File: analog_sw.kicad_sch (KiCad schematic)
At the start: 22 parts, among them J5 Conn_02x05_Top_Bottom, Q3 BC817-25LT1G, Q4 BC817-25LT1G, Q5 BC817-25LT1G, Q6 BC817-25LT1G, U7 LTV-247

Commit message: Fix LED driver bias, add ST pull-ups, name TPS7B91 NC pins
- Swap LED driver base resistors: 2.2k series (R18/R20/R23/R26) and
  10k pull-down (R17/R21/R24/R27). The old 10k/2.2k divider only gave
  ~0.6 V at the base, so the NPNs never turned on.
- Add 10k pull-ups R29-R32 from IO2-IO5 to +3V3 for the open-drain ST
  outputs of the TPS1H100-Q1 switches on the output module.
- Name TPS7B91 pins 3 and 4 "NC" (datasheet: not internally connected).

ERC violation count unchanged (45, all pre-existing).

Co-Authored-By: Claude Opus 5.5 <noreply@anthropic.com>
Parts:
- R17, R21, R24, R27: value 2.2k -> 10k
- R18, R20, R23, R26: value 10k -> 2.2k
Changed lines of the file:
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@@
 			)
 		)
-		(property "Value" "2.2k"
+		(property "Value" "10k"
 			(at 135.128 72.898 0)
 			(effects
@@
 			)
 		)
-		(property "Value" "10k"
+		(property "Value" "2.2k"
 			(at 134.62 127 90)
 			(effects
@@
 			)
 		)
-		(property "Value" "2.2k"
+		(property "Value" "10k"
 			(at 135.128 137.668 0)
 			(effects
@@
 			)
 		)
-		(property "Value" "10k"
+		(property "Value" "2.2k"
 			(at 134.62 62.23 90)
 			(effects
@@
 			)
 		)
-		(property "Value" "2.2k"
+		(property "Value" "10k"
 			(at 135.128 41.148 0)
 			(effects
@@
 			)
 		)
-		(property "Value" "10k"
+		(property "Value" "2.2k"
 			(at 134.62 93.98 90)
 			(effects
@@
 			)
 		)
-		(property "Value" "10k"
+		(property "Value" "2.2k"
 			(at 134.62 30.48 90)
 			(effects
@@
 			)
 		)
-		(property "Value" "2.2k"
+		(property "Value" "10k"
 			(at 135.128 104.648 0)
 			(effects

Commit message: Apply JLCPCB BOM audit fixes and add module ID / switch sense
- Remove CH340C and auto-reset circuit; USB-C goes to native USB
  (IO19 = D-, IO20 = D+). UART0 left unconnected.
- USB-C: HRO TYPE-C-31-M-12 (shell pins renumbered SH to match footprint).
- F1/F3: 1812L050/60GR (60 V, 500 mA hold); old part was rated 30 V max.
- D2/D3/D11: DSK16 (60 V) replacing out-of-stock DSS14U.
- D9: PESD2CAN replacing unavailable ESDCAN01-2BWY (SOT-23).
- L1: SWPA6045S8R2MT (Isat 3.9 A > LMR51610 peak limit 1.95 A).
- Feedback divider 68k/22k (basic parts): Vout 3.27 V with Vref 0.8 V.
- Basic-library swaps: TS-1187A buttons, 0805 2.2uF/50V, 49.9 R,
  BC817-40.
- Move the ST pull-ups to the output module.
- Header pin 12 becomes MOD_ID (IO1, 10k pull-up).
- SW1-SW4 to IO14/IO15/IO16/IO21 with 10k pull-downs, so the firmware
  can read the physical switches.
- Add LCSC part numbers for changed parts and main ICs.

ERC: 38 violations (was 45), none new except a missing PWR_FLAG on
+3V3 now that the CH340C no longer drives it.

Co-Authored-By: Claude Opus 5.5 <noreply@anthropic.com>
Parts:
- Q3, Q4, Q5, Q6: value BC817-25LT1G -> BC817-40; LCSC (none) -> C20069155
- R19, R22, R25, R28: value 50 -> 49.9; LCSC (none) -> C25120
- U7: LCSC (none) -> C115451

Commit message: Harden inputs for 30 V, finish BOM swaps, clean up ERC
- Switch inputs R3/R4/R7/R8: 330 R -> 4.7k 1206. 2 mA at 10.5 V,
  6.1 mA / 0.18 W at 30 V. LTV-247 CTR >= 50 % at 5 mA, ~0.7x at 2 mA
  (datasheet fig. 10) -> >= 0.7 mA out vs 0.33 mA needed.
- D1: SMAJ30CA (clamp 48.4 V, below the 50 V input caps).
- D10: SMAJ18CA on NMEA 2000 NET-S (9-16 V); clamp 29.2 V protects the
  TPS7B91 (42 V abs max). SMAJ33CA clamped at 53 V.
- F2: SMD0805B050TF; D4-D6: PESD0402V05; J4: WJ15EDGVC-3.81-04P
  (MCV 1.5 clone, footprint kept - verify against datasheet).
- ERC: PWR_FLAGs on +3V3, GND, VBUS, buck VIN, CAN LDO input, GND_CAN;
  LMR51610 symbol CB/FB/SW pins passive; spare GPIOs no-connect;
  orphaned CH340 GND symbol and IO18 stub removed; LED_C stub wires
  trimmed to their labels.

Netlist connectivity identical to previous commit. ERC: 8 left, all
lib_symbol_mismatch (BC817, LTV-247) - use Update Symbols from Library.

Co-Authored-By: Claude Opus 5.5 <noreply@anthropic.com>
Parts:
- R3, R4, R7, R8: value 330 -> 4.7k; footprint Resistor_SMD:R_0603_1608Metric -> Resistor_SMD:R_1206_3216Metric; LCSC (none) -> C17936
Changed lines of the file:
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@@
 	(wire
 		(pts
-			(xy 127 57.15)
+			(xy 128.27 57.15)
 			(xy 139.7 57.15)
 		)
@@
 	(wire
 		(pts
-			(xy 127 25.4)
+			(xy 128.27 25.4)
 			(xy 139.7 25.4)
 		)
@@
 	(wire
 		(pts
-			(xy 127 121.92)
+			(xy 128.27 121.92)
 			(xy 139.7 121.92)
 		)
@@
 	(wire
 		(pts
-			(xy 127 88.9)
+			(xy 128.27 88.9)
 			(xy 139.7 88.9)
 		)
@@
 			)
 		)
-		(property "Value" "330"
+		(property "Value" "4.7k"
 			(at 66.04 74.93 90)
 			(effects
@@
 			)
 		)
-		(property "Footprint" "Resistor_SMD:R_0603_1608Metric"
+		(property "Footprint" "Resistor_SMD:R_1206_3216Metric"
 			(at 66.04 80.518 90)
 			(effects
@@
 			)
 		)
+		(property "LCSC" "C17936"
+			(at 66.04 78.74 0)
+			(effects
+				(font
+					(size 1.27 1.27)
+				)
+				(hide yes)
+			)
+		)
 		(pin "1"
 		)
@@
 			)
 		)
-		(property "Value" "330"
+		(property "Value" "4.7k"
 			(at 66.04 88.9 90)
 			(effects
@@
 			)
 		)
-		(property "Footprint" "Resistor_SMD:R_0603_1608Metric"
+		(property "Footprint" "Resistor_SMD:R_1206_3216Metric"
 			(at 66.04 94.488 90)
 			(effects
@@
 			)
 		)
+		(property "LCSC" "C17936"
+			(at 66.04 92.71 0)
+			(effects
+				(font
+					(size 1.27 1.27)
+				)
+				(hide yes)
+			)
+		)
 		(pin "1"
 		)
@@
 			)
 		)
-		(property "Value" "330"
+		(property "Value" "4.7k"
 			(at 66.04 102.87 90)
 			(effects
@@
 			)
 		)
-		(property "Footprint" "Resistor_SMD:R_0603_1608Metric"
+		(property "Footprint" "Resistor_SMD:R_1206_3216Metric"
 			(at 66.04 108.458 90)
 			(effects
@@
 			)
 		)
+		(property "LCSC" "C17936"
+			(at 66.04 106.68 0)
+			(effects
+				(font
+					(size 1.27 1.27)
+				)
+				(hide yes)
+			)
+		)
 		(pin "1"
 		)
@@
 			)
 		)
-		(property "Value" "330"
+		(property "Value" "4.7k"
 			(at 66.04 116.84 90)
 			(effects
@@
 			)
 		)
-		(property "Footprint" "Resistor_SMD:R_0603_1608Metric"
+		(property "Footprint" "Resistor_SMD:R_1206_3216Metric"
 			(at 66.04 122.428 90)
 			(effects
@@
 			(at 66.04 120.65 0)
 			(effects
+				(font
+					(size 1.27 1.27)
+				)
+				(hide yes)
+			)
+		)
+		(property "LCSC" "C17936"
+			(at 66.04 120.65 0)
+			(effects

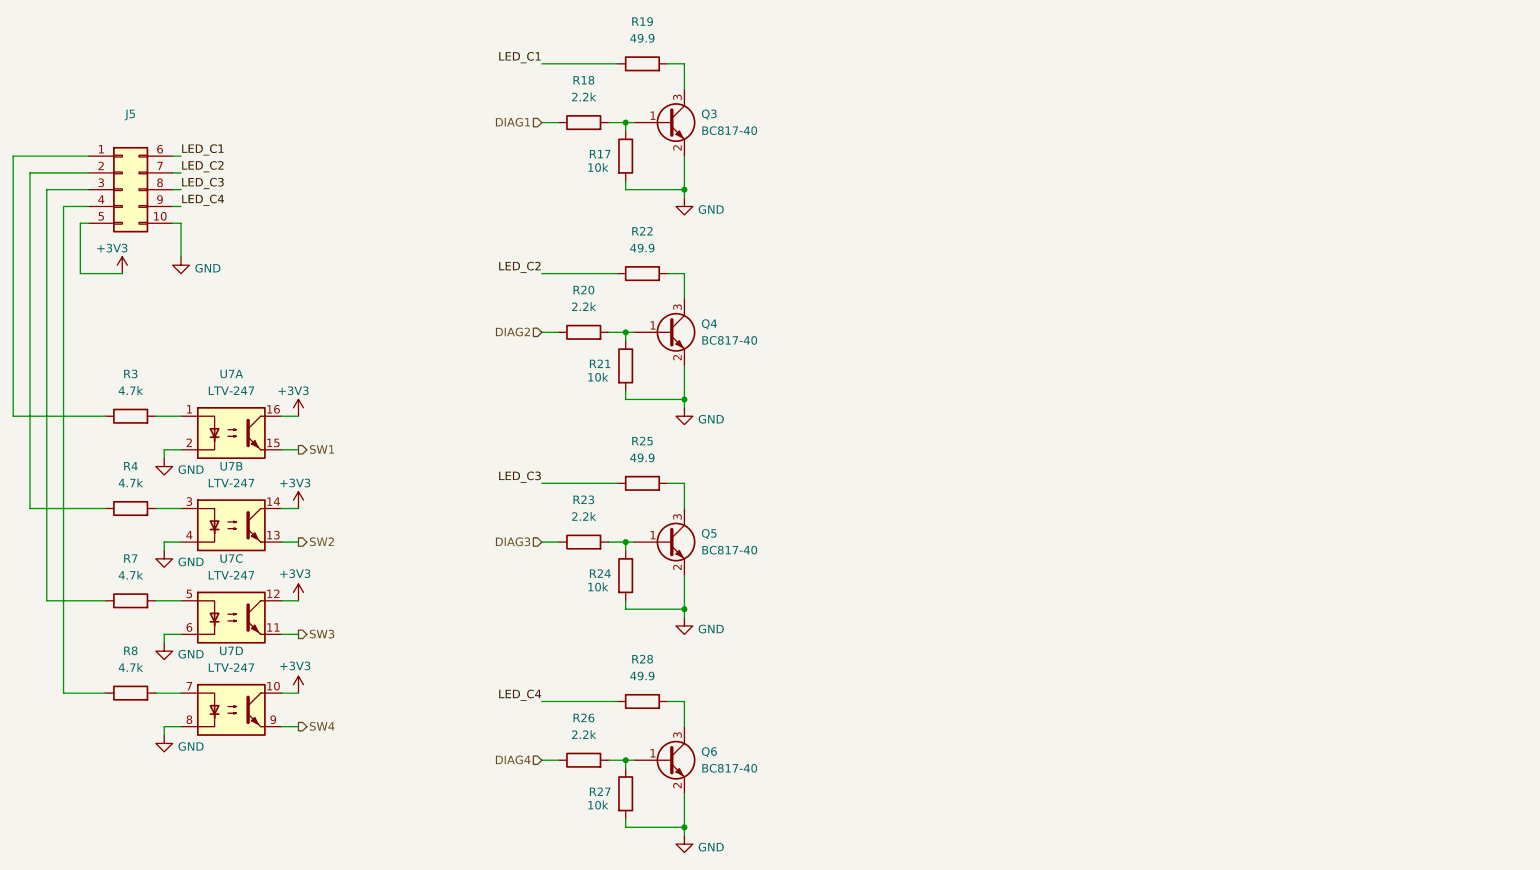
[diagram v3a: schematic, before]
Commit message: Replace opto switch inputs with protected direct inputs
The physical switch now drives the output EN without the LTV-247 and
without depending on the 3.3 V rail. Per input:
- SMAJ30CA TVS at J5 (surge/ESD on long switch cables)
- 4.7k 1206 load to GND (contact wetting 2.5 mA @ 12 V, 6.4 mA @ 30 V)
- 10k 1206 series + 4.7k/BZT52C3V3 divider-clamp + 100 nF:
  node ~3.2 V for 10.5-30 V in, EN threshold ~7.5 V, tau ~0.3 ms,
  negative spikes clamped by the Zener/TVS
- node -> existing BAT54C diode-OR -> SW_IN (module EN)
- R30-R33 now 10k series from the node to IO14/IO15/IO16/IO21,
  limiting back-feed into an unpowered ESP32 to ~0.3 mA

ERC: 4 left (BC817 lib_symbol_mismatch).

Co-Authored-By: Claude Opus 5.5 <noreply@anthropic.com>
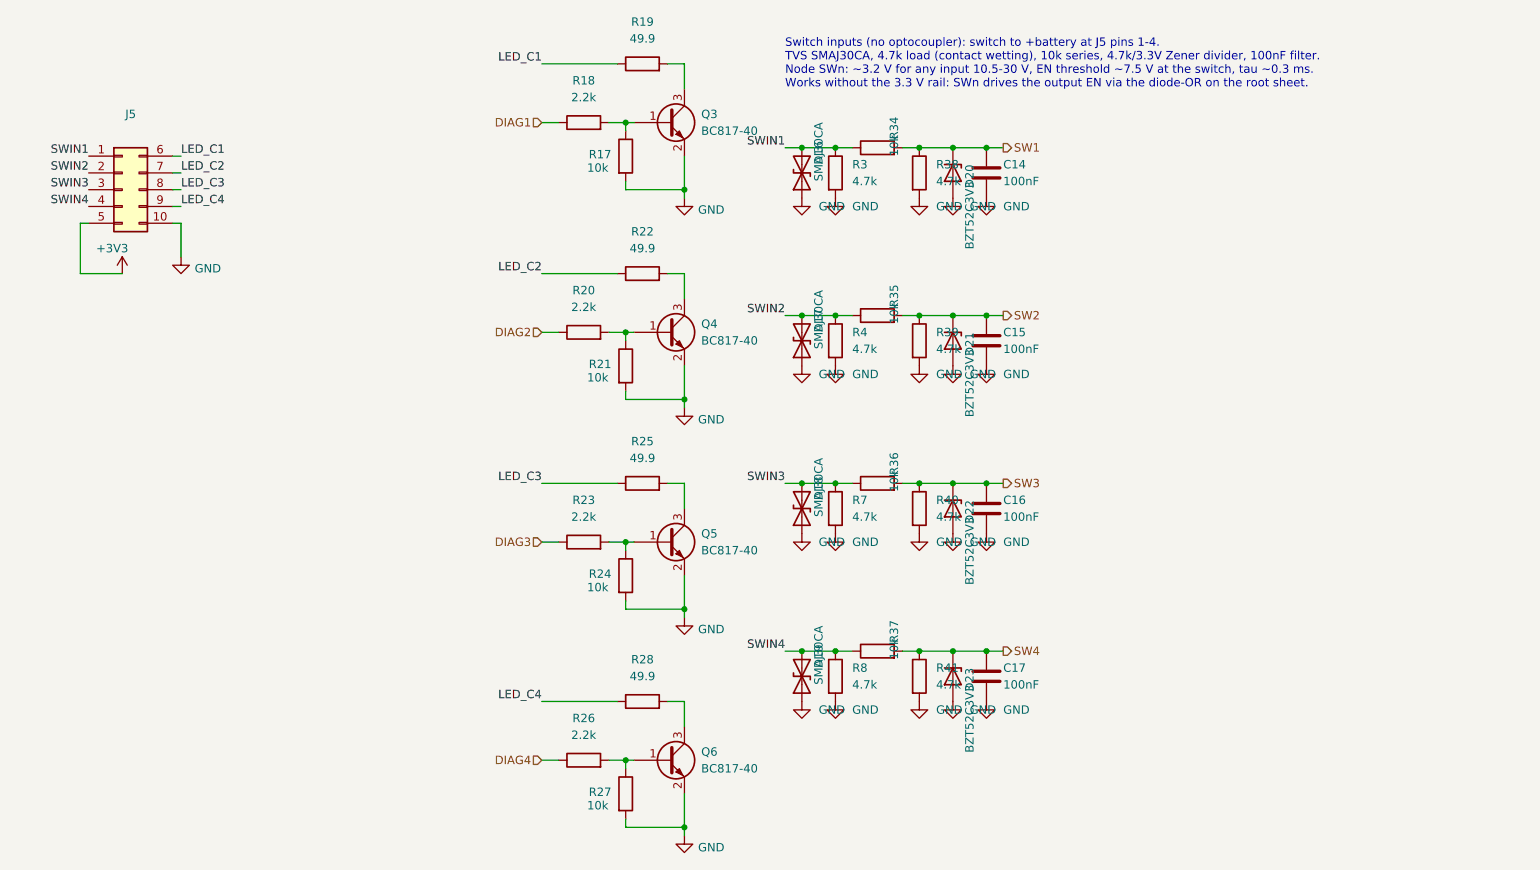
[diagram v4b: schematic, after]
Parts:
- removed U7: LTV-247, Package_SO:SOP-16_4.4x10.4mm_P1.27mm, symbol Isolator:LTV-247
- added C14, C15, C16, C17: 100nF, Capacitor_SMD:C_0402_1005Metric, symbol Device:C
- added D16, D17, D18, D19: SMAJ30CA, Diode_SMD:D_SMA, symbol Device:D_TVS
- added D20, D21, D22, D23: BZT52C3V3, Diode_SMD:D_SOD-123, symbol Device:D_Zener
- added R34, R35, R36, R37: 10k, Resistor_SMD:R_1206_3216Metric, symbol Device:R
- added R38, R39, R40, R41: 4.7k, Resistor_SMD:R_0402_1005Metric, symbol Device:R
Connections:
- net GND: now also R3.2, R4.2, R7.2, R8.2, C14.2, C15.2, C16.2, C17.2, D16.1 (A1), D17.1 (A1), D18.1 (A1), D19.1 (A1), D20.2 (A), D21.2 (A), D22.2 (A), D23.2 (A), R38.2, R39.2, R40.2, R41.2
- net SW1: now also C14.1, D20.1 (K), R34.2, R38.1
- net SW2: now also C15.1, D21.1 (K), R35.2, R39.1
- net SW3: now also C16.1, D22.1 (K), R36.2, R40.1
- net SW4: now also C17.1, D23.1 (K), R37.2, R41.1
- net SWIN1: now reaches J5.1 (Pin_1), R3.1
- net SWIN1: now also D16.2 (A2), R34.1
- net SWIN2: now reaches J5.2 (Pin_2), R4.1
- net SWIN2: now also D17.2 (A2), R35.1
- net SWIN3: now reaches J5.3 (Pin_3), R7.1
- net SWIN3: now also D18.2 (A2), R36.1
- net SWIN4: now reaches J5.4 (Pin_4), R8.1
- net SWIN4: now also D19.2 (A2), R37.1
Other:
- note added: "Switch inputs (no optocoupler): switch to +battery at J5 pins 1-4. TVS SMAJ30CA, 4.7k load (contact wetting), 10k series, 4.7k/3.3V Zener divider, 100nF filter. Node SWn: ~3.2 V for any input 10.5-30 V, EN threshold ~7.5 V at the switch, tau ~0.3 ms. Works without the 3.3 V rail: SWn drives the output EN via the diode-OR on the root sheet."
